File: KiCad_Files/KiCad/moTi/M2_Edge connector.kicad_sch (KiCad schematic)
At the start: 11 parts, among them Q2 NTK3043NT1G

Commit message: HW file update
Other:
- title: MosaicTimeSync -> moTi
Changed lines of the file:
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@@
 	(paper "A3")
 	(title_block
-		(title "MosaicTimeSync")
+		(title "moTi")
 		(date "2025-09-02")
 		(rev "01")
@@
 		(comment 2 "Programme under the Fundamental Elements ")
 		(comment 3 "co-funded by the European Union Agency for the Space ")
-		(comment 4 "MosaicTimeSync project has been documented by Septentrio")
+		(comment 4 "moTi project has been documented by Septentrio")
 	)
 	(rectangle

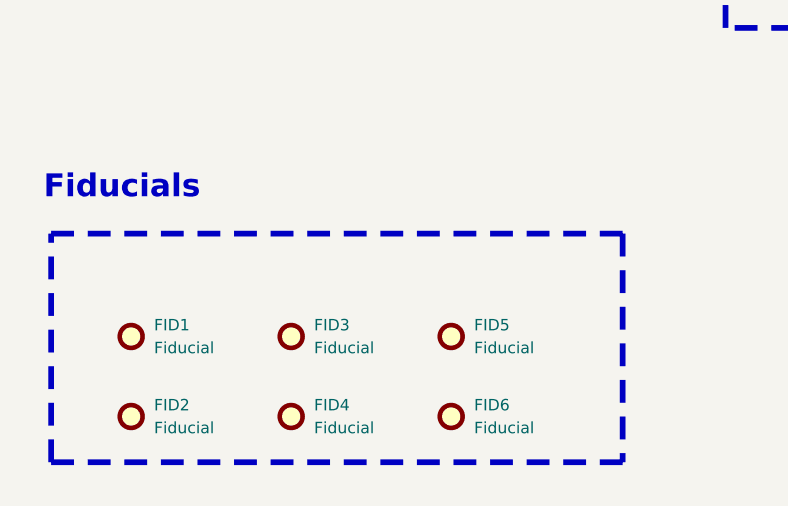
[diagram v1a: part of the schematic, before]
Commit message: I2C change
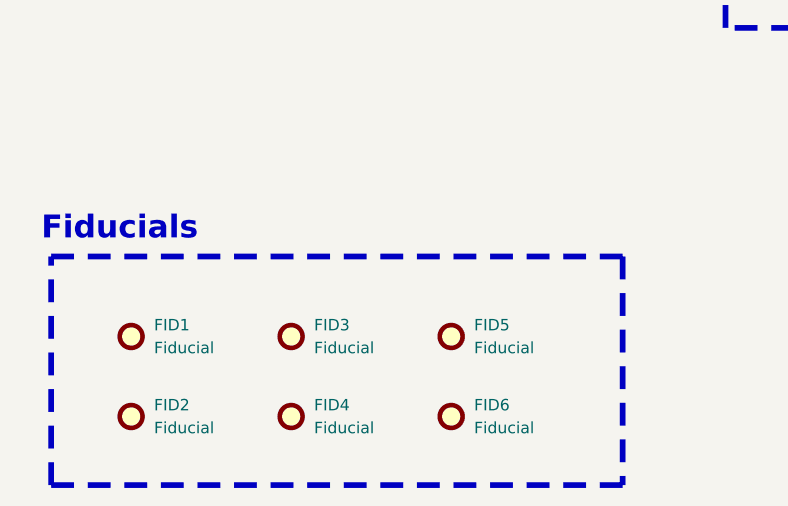
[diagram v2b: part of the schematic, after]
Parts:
- J2: value ~ -> (none)

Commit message: BOM update
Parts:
- removed R5, R6: 0, Resistor_SMD:R_0402_1005Metric, symbol Device:R
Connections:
- no-connect marks 20 -> 22

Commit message: general clean up
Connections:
- net VBAT: no longer names the net of J2.2 (3.3V/VBAT)
- net VBAT: no longer J2.4 (3.3V/VBAT)
- no-connect marks 22 -> 24
